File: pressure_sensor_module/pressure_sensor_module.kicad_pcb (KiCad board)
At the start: 4 copper layers, 31 x 29.5 mm, 7 parts, among them J1 Conn_02x04_Odd_Even, J2 Conn_02x07_Odd_Even, U1 MPX5100AP

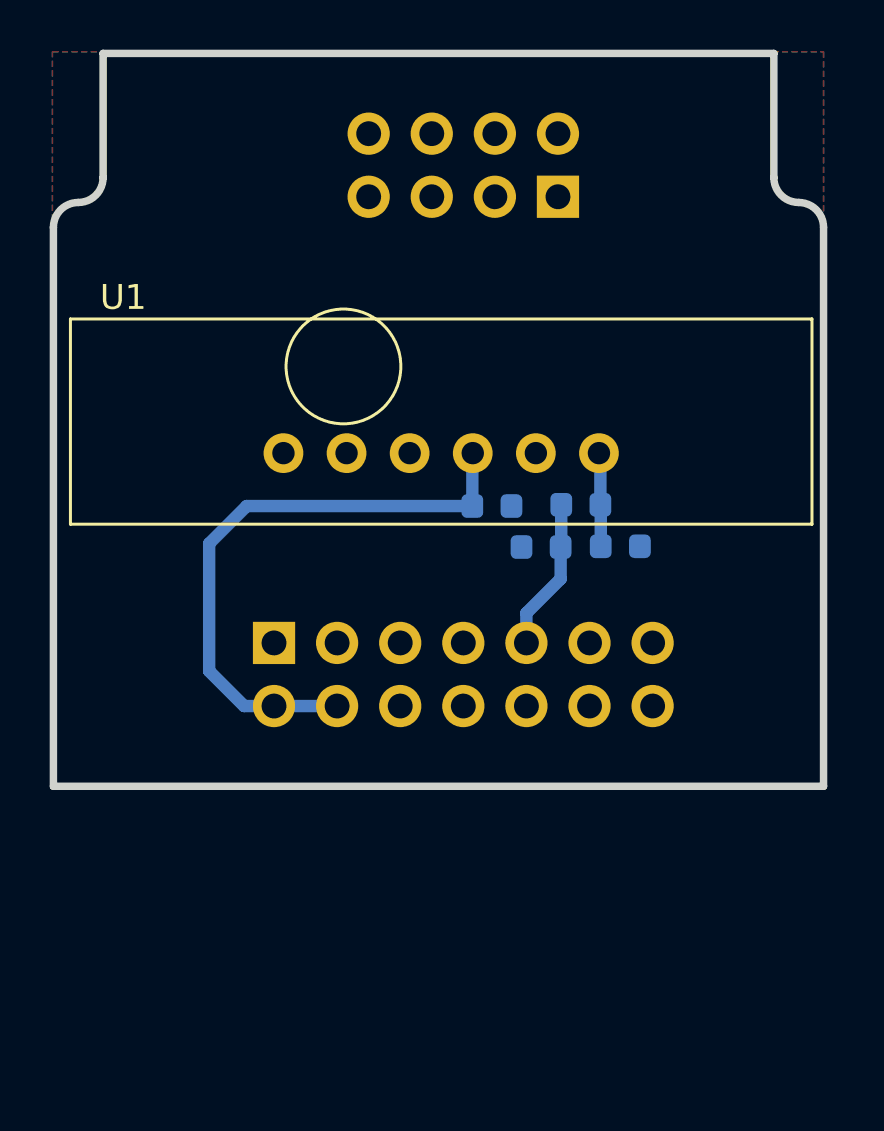
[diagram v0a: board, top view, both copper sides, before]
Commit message: - Added footprint MPX100 vertical - Modified pinHeader footprints to SMD
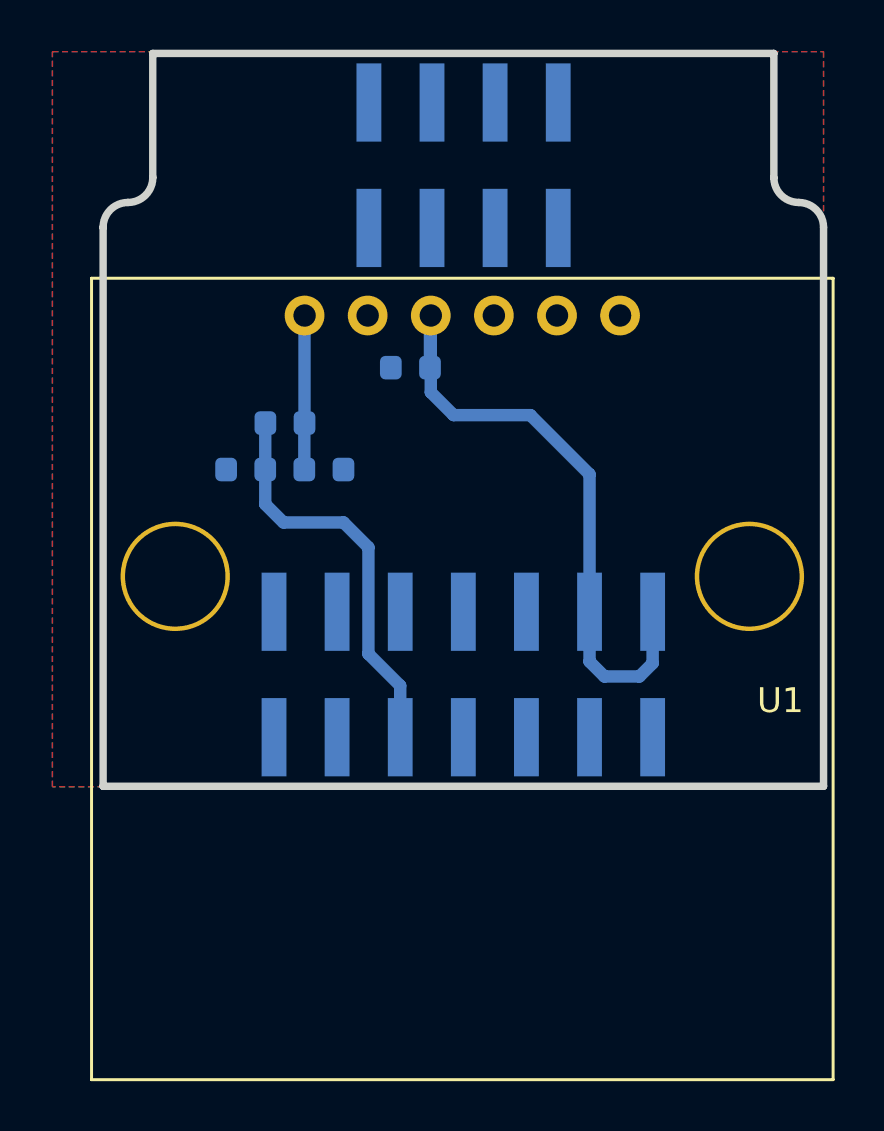
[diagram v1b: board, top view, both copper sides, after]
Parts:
- J1: footprint Connector_PinHeader_2.54mm:PinHeader_2x04_P2.54mm_Vertical -> Connector_PinHeader_2.54mm:PinHeader_2x04_P2.54mm_Vertical_SMD
- J2: footprint Connector_PinHeader_2.54mm:PinHeader_2x07_P2.54mm_Vertical -> Connector_PinHeader_2.54mm:PinHeader_2x07_P2.54mm_Vertical_SMD
- moved R1 12.4 mm to (105.8, 45.0)
- moved C2 12.3 mm to (107.3, 46.8)
- moved R2 12.3 mm to (104.2, 46.8)
- moved J2 7.73 mm to (113.0, 55.1), turned to 90 degrees
- moved C1 6.46 mm to (110.8, 42.7), turned to 180 degrees
- moved U1 6.29 mm to (112.9, 51.1), turned to 180 degrees
- moved J1 4.01 mm to (113.0, 34.6)
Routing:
- net /Analog: track 6.14 -> 16.3 mm
- net Net-(C2-Pad1): track 3.78 -> 6.20 mm
- net +5V: track 24.2 -> 25.6 mm
- net /SPI_CS: track 0.00 -> 1.20 mm
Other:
- board size 31 x 29.5 mm -> 29 x 29.5 mm
